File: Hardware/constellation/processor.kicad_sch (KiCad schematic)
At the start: 1 part, among them U1 STM32H723ZGTx

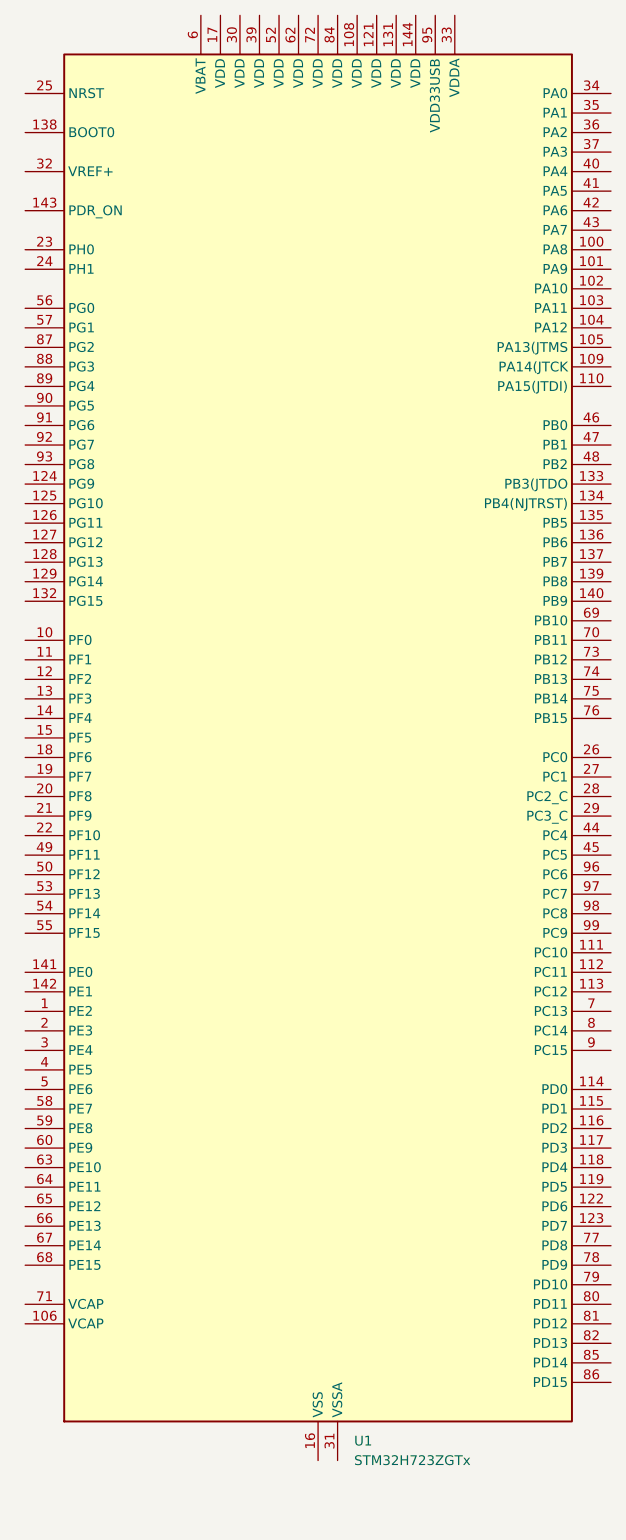
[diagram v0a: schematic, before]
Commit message: add pyro stuff, start system power
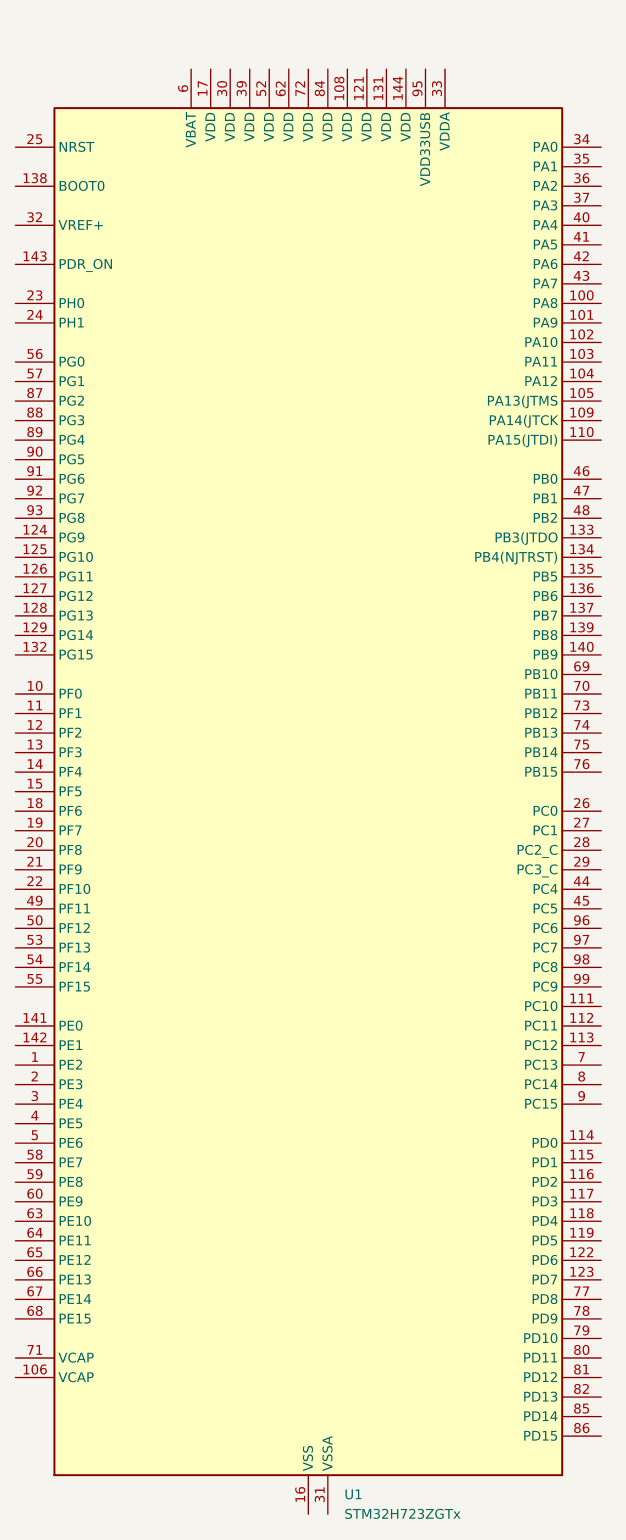
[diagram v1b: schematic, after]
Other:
- moved on the sheet: U1
